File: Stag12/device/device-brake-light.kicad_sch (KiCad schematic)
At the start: 2 parts

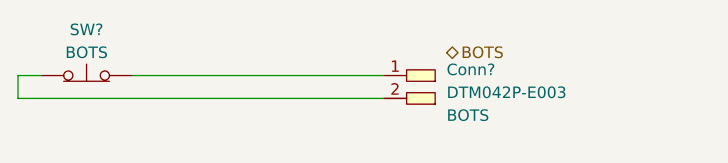
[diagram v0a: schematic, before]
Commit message: Changed filepaths
Makes graphical explorers a bit neater

TODO: Decide on new paths for each device (maybe geographical?)
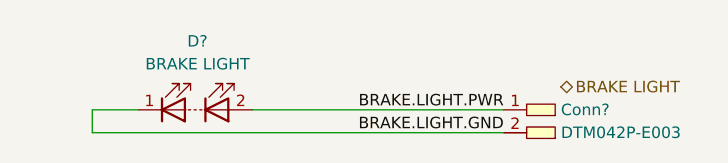
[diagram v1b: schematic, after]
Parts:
- removed Conn?: Deutsch_DTM_2P_Pin, symbol Connectors_SUFST:Deutsch_DTM_2P_Pin
- removed SW?: BOTS, symbol Switch:SW_Push_Open
- added Conn?: Deutsch_DTM_2P_Pin, symbol Connectors_SUFST:Deutsch_DTM_2P_Pin
- added D?: BRAKE LIGHT, symbol Device:LED_Series
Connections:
- new net BRAKE.LIGHT.GND: Conn?.2, D?.1 (K)
- new net BRAKE.LIGHT.PWR: Conn?.1, D?.2 (A)
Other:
- title: DEVICE - BOTS -> LOOM - BRAKE LIGHT
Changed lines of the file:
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@@
 	(paper "A4")
 	(title_block
-		(title "DEVICE - BOTS")
-	)
-	(wire
-		(pts
-			(xy 114.935 90.17) (xy 112.395 90.17)
-		)
-		(stroke
-			(width 0)
-			(type default)
-		)
-	)
-	(wire
-		(pts
-			(xy 112.395 92.71) (xy 153.035 92.71)
-		)
-		(stroke
-			(width 0)
-			(type default)
-		)
-	)
-	(wire
-		(pts
-			(xy 125.095 90.17) (xy 153.035 90.17)
-		)
-		(stroke
-			(width 0)
-			(type default)
-		)
-	)
-	(wire
-		(pts
-			(xy 112.395 90.17) (xy 112.395 92.71)
-		)
-		(stroke
-			(width 0)
-			(type default)
-		)
-	)
-	(hierarchical_label "BOTS"
-		(shape bidirectional)
-		(at 160.02 87.63 0)
+		(title "LOOM - BRAKE LIGHT")
+	)
+	(wire
+		(pts
+			(xy 125.73 93.98) (xy 120.65 93.98)
+		)
+		(stroke
+			(width 0)
+			(type default)
+		)
+	)
+	(wire
+		(pts
+			(xy 120.65 96.52) (xy 166.37 96.52)
+		)
+		(stroke
+			(width 0)
+			(type default)
+		)
+	)
+	(wire
+		(pts
+			(xy 120.65 93.98) (xy 120.65 96.52)
+		)
+		(stroke
+			(width 0)
+			(type default)
+		)
+	)
+	(wire
+		(pts
+			(xy 138.43 93.98) (xy 166.37 93.98)
+		)
+		(stroke
+			(width 0)
+			(type default)
+		)
+	)
+	(label "BRAKE.LIGHT.GND"
+		(at 166.37 96.52 180)
 		(effects
 			(font
 				(size 1.27 1.27)
 			)
+			(justify right bottom)
+		)
+	)
+	(label "BRAKE.LIGHT.PWR"
+		(at 166.37 93.98 180)
+		(effects
+			(font
+				(size 1.27 1.27)
+			)
+			(justify right bottom)
+		)
+	)
+	(hierarchical_label "BRAKE LIGHT"
+		(shape bidirectional)
+		(at 172.72 91.44 0)
+		(effects
+			(font
+				(size 1.27 1.27)
+			)
 			(justify left)
 		)
@@
 	(symbol
 		(lib_id "Connectors_SUFST:Deutsch_DTM_2P_Pin")
-		(at 154.94 97.155 180)
+		(at 168.275 100.965 180)
 		(unit 1)
 		(exclude_from_sim no)
@@
 		(fields_autoplaced yes)
 		(property "Reference" "Conn?"
-			(at 160.02 89.535 0)
+			(at 172.72 93.98 0)
 			(effects
 				(font
@@
 		)
 		(property "Value" "Deutsch_DTM_2P_Pin"
-			(at 154.94 97.155 0)
+			(at 168.275 100.965 0)
 			(effects
 				(font
@@
 		)
 		(property "Footprint" ""
-			(at 154.94 95.25 0)
+			(at 168.275 99.06 0)
 			(effects
 				(font
@@
 		)
 		(property "Datasheet" ""
-			(at 154.94 95.25 0)
+			(at 168.275 99.06 0)
 			(effects
 				(font
@@
 		)
 		(property "Description" ""
-			(at 154.94 97.155 0)
+			(at 168.275 100.965 0)
 			(effects
 				(font
@@
 		)
 		(property "P/N" "DTM042P-E003"
-			(at 160.02 92.075 0)
+			(at 172.72 96.52 0)
 			(effects
 				(font
@@
 			)
 		)
-		(property "Conn Name" "BOTS"
-			(at 160.02 94.615 0)
-			(effects
-				(font
-					(size 1.27 1.27)
-				)
-				(justify right)
-			)
-		)
 		(pin "1"
 		)
@@
 		)
 		(instances
-			(project "Stag11"
-				(path "/03011643-0690-4b85-ab78-d6a62dae52b1/070b8217-88a3-4264-8b23-f32d97ad3850"
+			(project "Stag12"
+				(path "/03011643-0690-4b85-ab78-d6a62dae52b1/fbcd0b6d-423f-4780-bac5-0cf90db94f41"
 					(reference "Conn?")
 					(unit 1)
@@
 	)
 	(symbol
-		(lib_id "Switch:SW_Push_Open")
-		(at 120.015 90.17 0)
+		(lib_id "Device:LED_Series")
+		(at 132.08 93.98 0)
 		(unit 1)
 		(exclude_from_sim no)
@@
 		(dnp no)
 		(fields_autoplaced yes)
-		(property "Reference" "SW?"
-			(at 120.015 85.09 0)
-			(effects
-				(font
-					(size 1.27 1.27)
-				)
-			)
-		)
-		(property "Value" "BOTS"
-			(at 120.015 87.63 0)
+		(property "Reference" "D?"
+			(at 132.334 86.36 0)
+			(effects
+				(font
+					(size 1.27 1.27)
+				)
+			)
+		)
+		(property "Value" "BRAKE LIGHT"
+			(at 132.334 88.9 0)
 			(effects
 				(font
@@
 		)
 		(property "Footprint" ""
-			(at 120.015 85.09 0)
+			(at 129.54 93.98 0)
 			(effects
 				(font
@@
 		)
 		(property "Datasheet" "~"
-			(at 120.015 85.09 0)
+			(at 129.54 93.98 0)
 			(effects
 				(font
@@
 		)
 		(property "Description" ""
-			(at 120.015 90.17 0)
-			(effects
-				(font
-					(size 1.27 1.27)
-				)
-				(hide yes)
-			)
-		)
-		(property "Conn Name" ""
-			(at 120.015 86.36 0)
-			(effects
-				(font
-					(size 1.27 1.27)
-				)
+			(at 132.08 93.98 0)
+			(effects
+				(font
+					(size 1.27 1.27)
+				)
+				(hide yes)
 			)
 		)
@@
 		)
 		(instances
-			(project "Stag11"
-				(path "/03011643-0690-4b85-ab78-d6a62dae52b1/070b8217-88a3-4264-8b23-f32d97ad3850"
-					(reference "SW?")
+			(project "Stag12"
+				(path "/03011643-0690-4b85-ab78-d6a62dae52b1/fbcd0b6d-423f-4780-bac5-0cf90db94f41"
+					(reference "D?")
 					(unit 1)
 				)
